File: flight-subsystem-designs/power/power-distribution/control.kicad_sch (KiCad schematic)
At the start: 17 parts, among them SW1 SW_Push, U11 MAX706RESA, U15 MR25H256ACDF, U19 STM32L431CBTx, Y1 Crystal_GND24

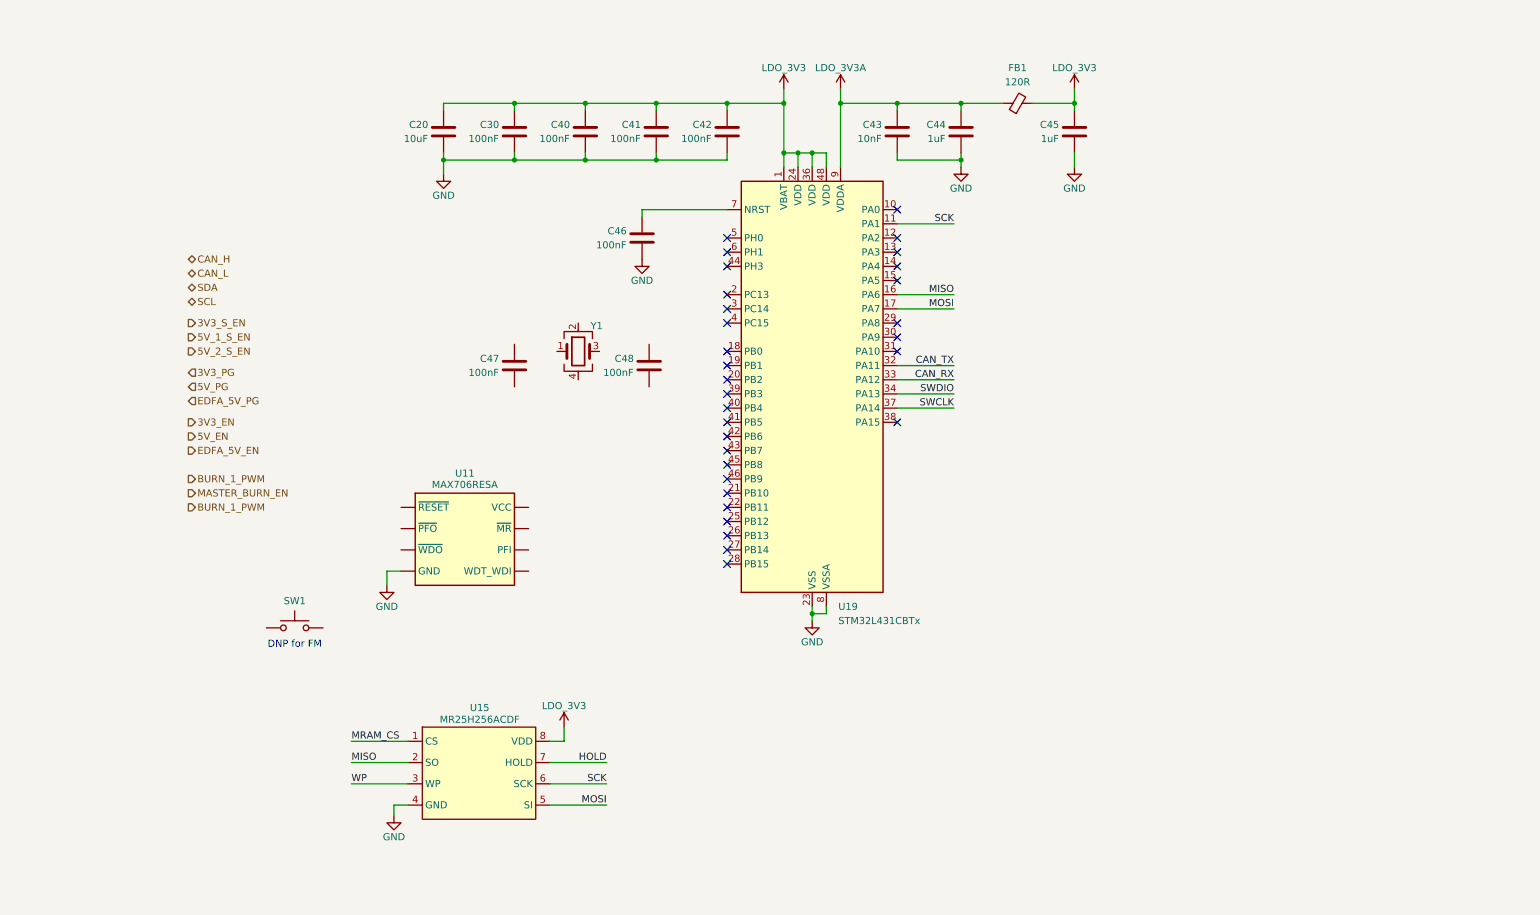
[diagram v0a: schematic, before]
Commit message: feat: PDU 4.0.0 (WIP)
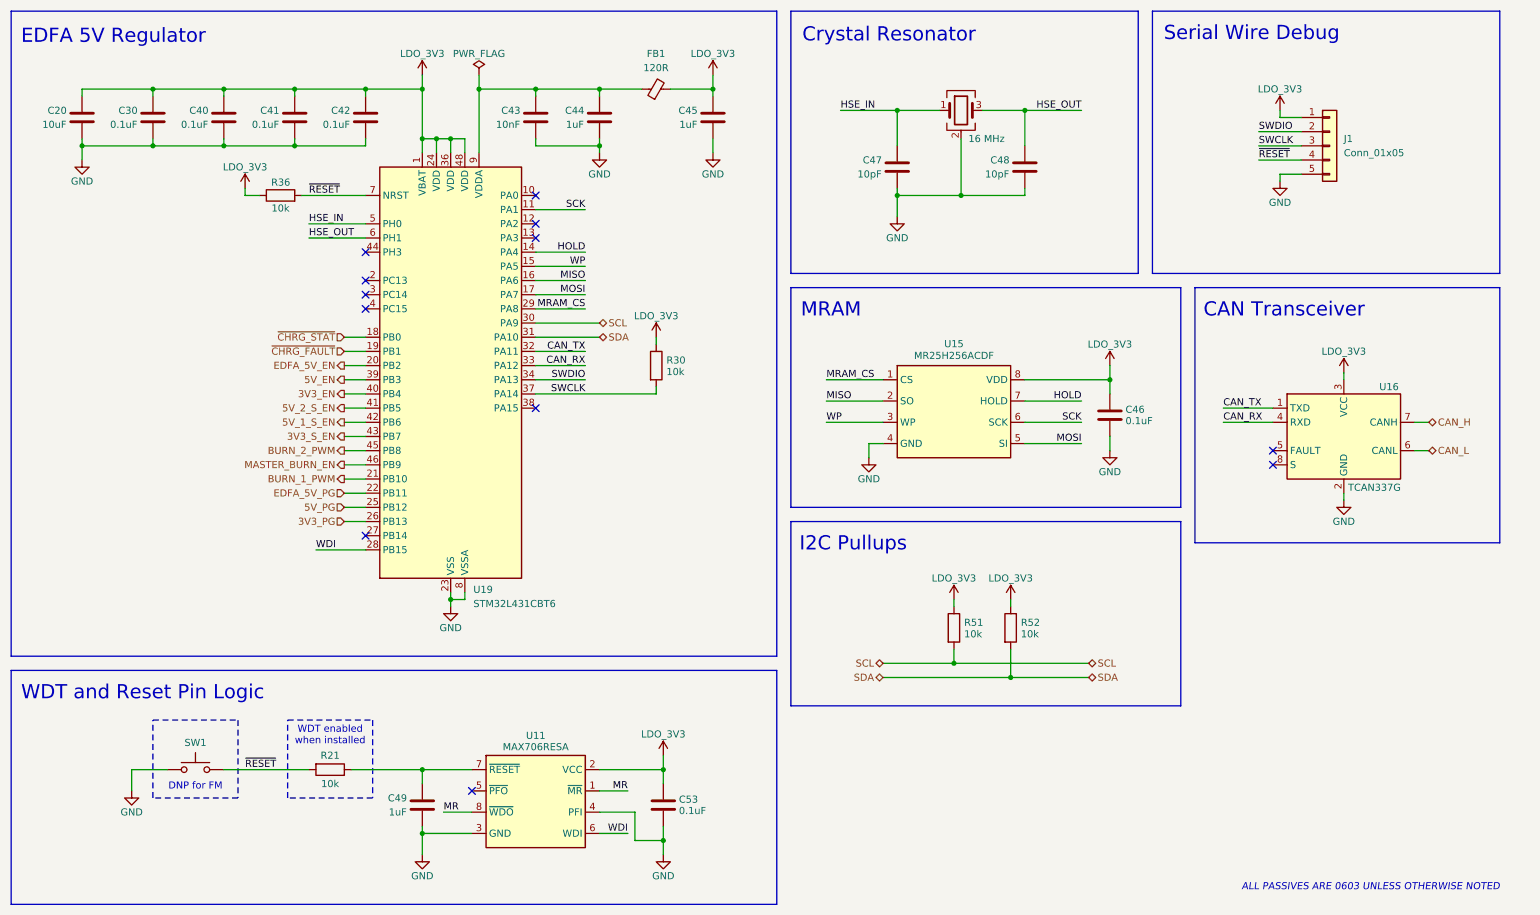
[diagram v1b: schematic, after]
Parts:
- added C49: 1uF, Capacitor_SMD:C_0603_1608Metric, symbol Device:C
- added C53: 0.1uF, Capacitor_SMD:C_0603_1608Metric, symbol Device:C
- added J1: Conn_01x05, Connector_PinHeader_2.54mm:PinHeader_1x05_P2.54mm_Vertical, symbol Connector_Generic:Conn_01x05
- added R21, R30, R36, R51, R52: 10k, Resistor_SMD:R_0603_1608Metric, symbol Device:R
- added U16: TCAN337G, Package_SO:SOIC-8_3.9x4.9mm_P1.27mm, symbol Interface_CAN_LIN:TCAN337G
- C30, C40, C41, C42, C46: value 100nF -> 0.1uF
- C47, C48: value 100nF -> 10pF
- FB1: footprint (none) -> Inductor_SMD:L_0805_2012Metric
- SW1: footprint (none) -> Button_Switch_SMD:SW_SPST_B3U-1000P
- U19: value STM32L431CBTx -> STM32L431CBT6
- Y1: value Crystal_GND24 -> 16 MHz; footprint (none) -> Crystal:Crystal_SMD_3225-4Pin_3.2x2.5mm
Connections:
- net 3V3_EN: now also U19.40 (PB4)
- net 3V3_PG: now also U19.26 (PB13)
- net 3V3_S_EN: now also U19.43 (PB7)
- net 5V_1_S_EN: now also U19.42 (PB6)
- net 5V_2_S_EN: now also U19.41 (PB5)
- net 5V_EN: now also U19.39 (PB3)
- net 5V_PG: now also U19.25 (PB12)
- net BURN_1_PWM: now also U19.21 (PB10)
- net CAN_H: now also U16.7 (CANH)
- net CAN_L: now also U16.6 (CANL)
- net CAN_RX: now also U16.4 (RXD)
- net CAN_TX: now also U16.1 (TXD)
- net EDFA_5V_EN: now also U19.20 (PB2)
- net EDFA_5V_PG: now also U19.22 (PB11)
- net GND: now also C46.1, C47.2, C48.2, SW1.1, U11.3 (GND), U11.4 (PFI), Y1.2 (G), Y1.4 (G), C49.2, C53.1, J1.5 (Pin_5), U16.2 (GND); no longer C46.2, U11. (WDT_WDI)
- net HOLD: now also U19.14 (PA4)
- net LDO_3V3: now also C46.2, U11.2 (VCC), C53.2, J1.1 (Pin_1), R30.1, R36.1, R51.1, R52.1, U16.3 (VCC)
- net MASTER_BURN_EN: now also U19.46 (PB9)
- net MRAM_CS: now also U19.29 (PA8)
- net SCL: now also U19.30 (PA9), R51.2
- net SDA: now also U19.31 (PA10), R52.2
- net SWCLK: now also J1.3 (Pin_3), R30.2
- net SWDIO: now also J1.2 (Pin_2)
- net WP: now also U19.15 (PA5)
- net ~{RESET}: now reaches U19.7 (NRST)
- net ~{RESET}: now also SW1.2, J1.4 (Pin_4), R21.2, R36.2; no longer C46.1
- net HSE_OUT: now reaches C48.1
- net HSE_OUT: now also U19.6 (PH1), Y1.3
- net HSE_IN: now reaches C47.1
- net HSE_IN: now also U19.5 (PH0), Y1.1
- net ~{CHRG_STAT}: now reaches U19.18 (PB0)
- net ~{CHRG_FAULT}: now reaches U19.19 (PB1)
- net WDI: now reaches U19.28 (PB15)
- net WDI: now also U11.6 (WDI)
- net BURN_2_PWM: now reaches U19.45 (PB8)
- net LDO_3V3A: no longer names the net of C43.1, C44.1, FB1.1, U19.9 (VDDA)
- new net: C49.1, R21.1, U11.7 (~{RESET})
- new net MR: U11.1 (~{MR}), U11.8 (~{WDO})
- no-connect marks 31 -> 12
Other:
- note added: "ALL PASSIVES ARE 0603 UNLESS OTHERWISE NOTED"
- note added: "CAN Transceiver"
- note added: "Crystal Resonator"
- note added: "EDFA 5V Regulator"
- note added: "I2C Pullups"
- note added: "MRAM"
- note added: "Serial Wire Debug"
- note added: "WDT and Reset Pin Logic"
- note added: "WDT enabled when installed"
- moved on the sheet: C20, C30, C40, C41, C42, C43, C44, C45, C47, C48, FB1, SW1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

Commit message: shi
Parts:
- removed C48: 10pF, Capacitor_SMD:C_0603_1608Metric, symbol Device:C
- removed Y1: 16 MHz, Crystal:Crystal_SMD_3225-4Pin_3.2x2.5mm, symbol Device:Crystal_GND24
- added C39: 0.1uF, Capacitor_SMD:C_0603_1608Metric, symbol Device:C
- added D18: GREEN, LED_SMD:LED_0603_1608Metric, symbol Device:LED
- added R44: 50, Resistor_SMD:R_0603_1608Metric, symbol Device:R
- added R54: 150, Resistor_SMD:R_0603_1608Metric, symbol Device:R
- added U21: SIT2024B, Package_TO_SOT_SMD:SOT-23-5, symbol pdu:SIT2024B
- C47: value 10pF -> 0.1uF
- J1: footprint Connector_PinHeader_2.54mm:PinHeader_1x05_P2.54mm_Vertical -> Connector_Molex:Molex_PicoBlade_53047-0510_1x05_P1.25mm_Vertical
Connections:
- net 3V3_EN: now also U19.41 (PB5); no longer U19.40 (PB4)
- net 3V3_PG: now also U19.40 (PB4); no longer U19.26 (PB13)
- net 3V3_S_EN: now also U19.42 (PB6); no longer U19.43 (PB7)
- net 5V_1_S_EN: now also U19.21 (PB10); no longer U19.42 (PB6)
- net 5V_2_S_EN: now also U19.25 (PB12); no longer U19.41 (PB5)
- net 5V_EN: now also U19.26 (PB13); no longer U19.39 (PB3)
- net 5V_PG: now also U19.13 (PA3); no longer U19.25 (PB12)
- net BURN_1_PWM: now also U19.29 (PA8); no longer U19.21 (PB10)
- net BURN_2_PWM: now also U19.27 (PB14); no longer U19.45 (PB8)
- net EDFA_5V_EN: now also U19.22 (PB11); no longer U19.20 (PB2)
- net EDFA_5V_PG: now also U19.12 (PA2); no longer U19.22 (PB11)
- net GND: now also C47.1, C39.2, R54.2, U21.1 (GND); no longer C47.2
- net HSE_IN: now also R44.2; no longer C47.1
- net LDO_3V3: now also C47.2, C39.1, U21.3 (OE/NC), U21.4 (VDD)
- net MASTER_BURN_EN: now also U19.28 (PB15); no longer U19.46 (PB9)
- net MRAM_CS: now also U19.20 (PB2); no longer U19.29 (PA8)
- net WDI: now also U19.43 (PB7); no longer U19.28 (PB15)
- net at U19.38 (PA15): now also D18.2 (A)
- net HSE_OUT: no longer names the net of U19.6 (PH1)
- new net: R44.1, U21.5 (OUT)
- new net: D18.1 (K), R54.1
- no-connect marks 12 -> 9
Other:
- note added: "MEMS Oscillator"
- note removed: "Crystal Resonator"
- moved on the sheet: C46, C49, C53, R21, R30, SW1, U11, U15
